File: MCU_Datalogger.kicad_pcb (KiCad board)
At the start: 2 copper layers, 29 parts, among them J1 Conn_01x04_Pin, J2 Conn_01x04_Pin, J3 Conn_01x09_Pin, J4 Conn_02x03_Odd_Even, U1 24LC1025, U2 24LC1025, U3 DS1337S_, U4 ATMEGA328P-AN, Y1 16 MHz, Y2 32.768 KHz

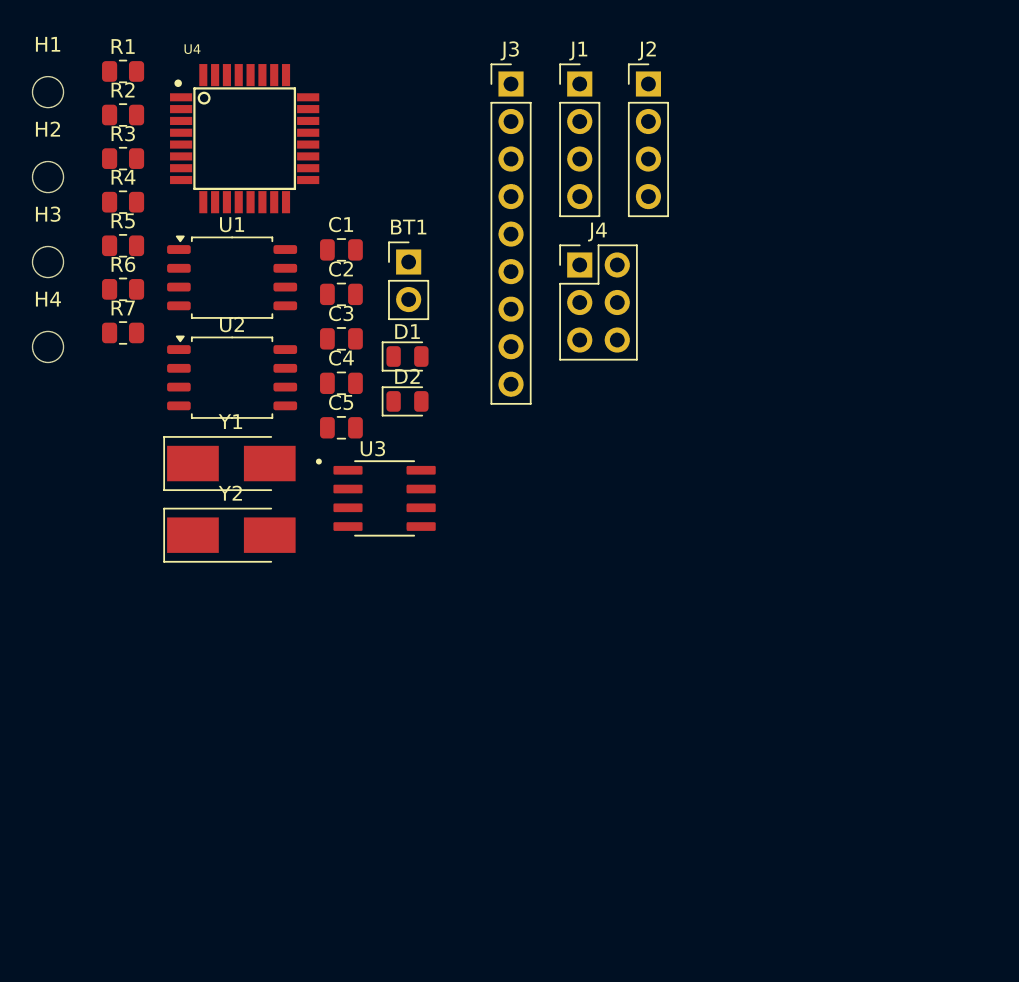
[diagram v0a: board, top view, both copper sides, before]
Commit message: Placed Components in 2 layer PCB.
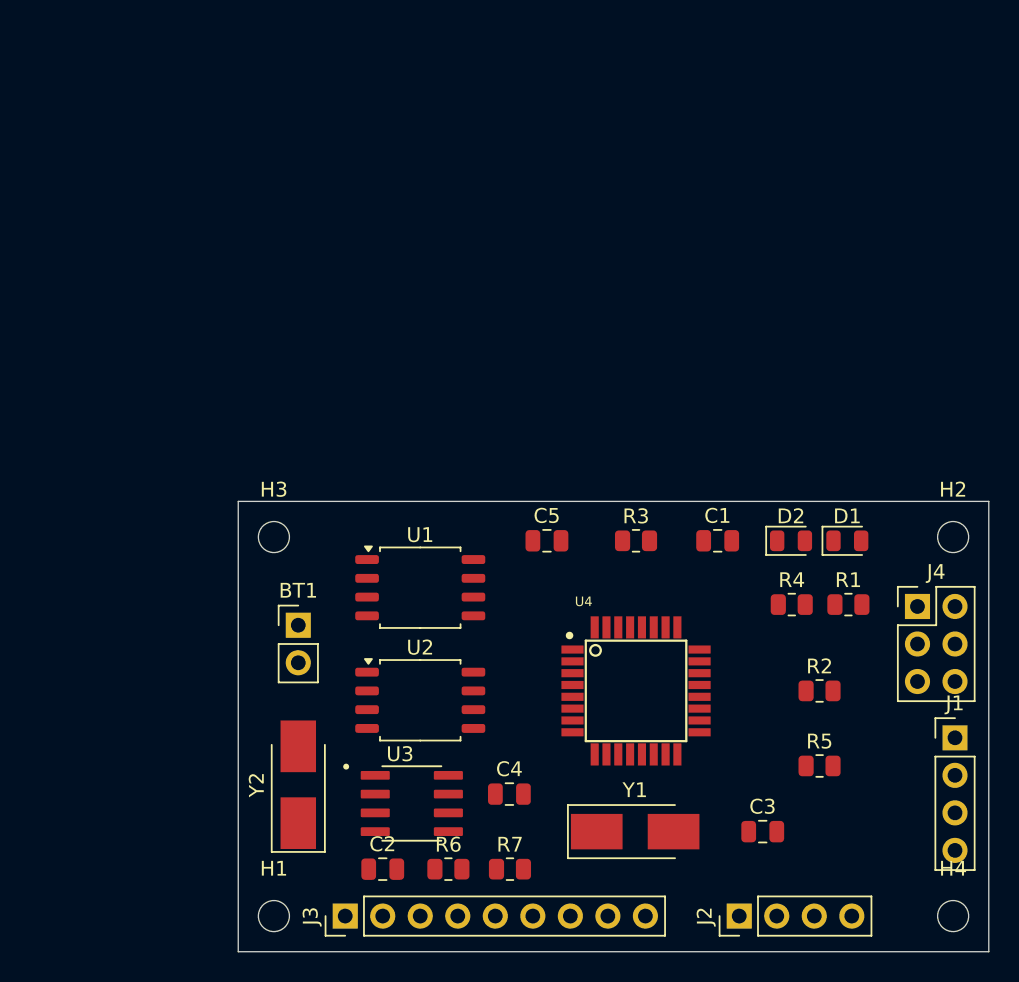
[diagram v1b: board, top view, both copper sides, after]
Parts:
- moved H4 72.4 mm to (173.9, 125.1)
- moved H2 65.9 mm to (173.9, 99.4)
- moved R2 61.2 mm to (164.8, 109.9)
- moved R1 60.9 mm to (166.8, 104.0)
- moved R5 58.8 mm to (164.8, 114.9)
- moved H1 57.8 mm to (127.9, 125.1)
- moved J3 57.4 mm to (132.7, 125.1), turned to 90 degrees
- moved J2 56.7 mm to (159.4, 125.1), turned to 90 degrees
- moved R4 52.8 mm to (162.9, 104.0)
- moved J1 51.0 mm to (174.0, 113.0)
- moved U4 45.8 mm to (152.4, 109.9)
- moved R6 45.0 mm to (139.7, 121.9)
- moved R7 44.8 mm to (143.9, 121.9)
- moved C3 43.9 mm to (161.0, 119.4)
- moved R3 43.3 mm to (152.4, 99.7)
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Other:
- board outline added: 50.8 x 30.5 mm

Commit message: Two Layer PCB Routing Done.
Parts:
- moved R7 16.5 mm to (143.8, 105.4)
- moved R6 8.19 mm to (143.8, 114.8)
- moved C4 7.33 mm to (150.9, 118.9)
- moved Y1 5.08 mm to (157.4, 119.4)
- moved C3 3.81 mm to (164.8, 119.4)
- moved U4 1.46 mm to (153.8, 109.5)
- moved U1 1.38 mm to (137.3, 101.6)
- moved U2 1.38 mm to (137.3, 109.2)
- moved U3 1.27 mm to (137.2, 116.2)
- moved R5 1.01 mm to (165.6, 114.3)
- moved D1 0.94 mm to (167.6, 99.7)
- moved R1 0.87 mm to (167.6, 104.0)
- moved Y2 0.68 mm to (129.0, 115.8)
- moved BT1 0.63 mm to (128.9, 105.4)
- moved C2 0.51 mm to (135.2, 121.4), turned to 180 degrees
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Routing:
- net GND: track 0.00 -> 203.2 mm, vias 0 -> 10
- net /Vcc: track 0.00 -> 167.8 mm, vias 0 -> 10
- net /SCK: track 0.00 -> 106.9 mm, vias 0 -> 12
- net Net-(U4-PB6): track 0.00 -> 95.7 mm, vias 0 -> 6
- net /SDA: track 0.00 -> 93.8 mm, vias 0 -> 6
- net Net-(BT1-+): track 0.00 -> 91.1 mm, vias 0 -> 3
- net /RX: track 0.00 -> 48.3 mm
- net /TX: track 0.00 -> 45.7 mm
- net /MOSI: track 0.00 -> 44.0 mm, vias 0 -> 1
- net /RESET: track 0.00 -> 43.8 mm, vias 0 -> 5
- net Net-(U4-PB7): track 0.00 -> 39.6 mm, vias 0 -> 2
- net /D2: track 0.00 -> 32.7 mm, vias 0 -> 2
- net /D3: track 0.00 -> 27.6 mm, vias 0 -> 2
- net Net-(U4-AREF): track 0.00 -> 26.9 mm
- net /D4: track 0.00 -> 24.5 mm, vias 0 -> 2
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
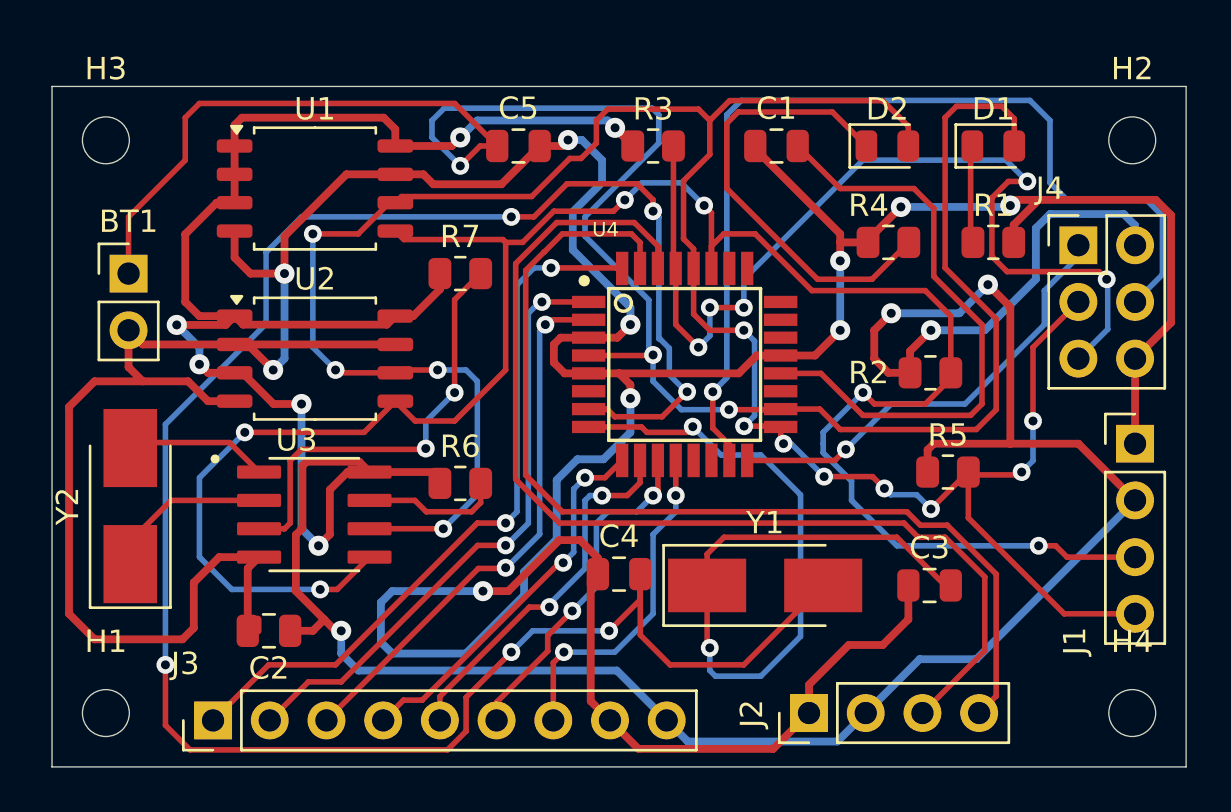
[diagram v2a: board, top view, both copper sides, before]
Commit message: Two Layer PCB done along with 3d Models.
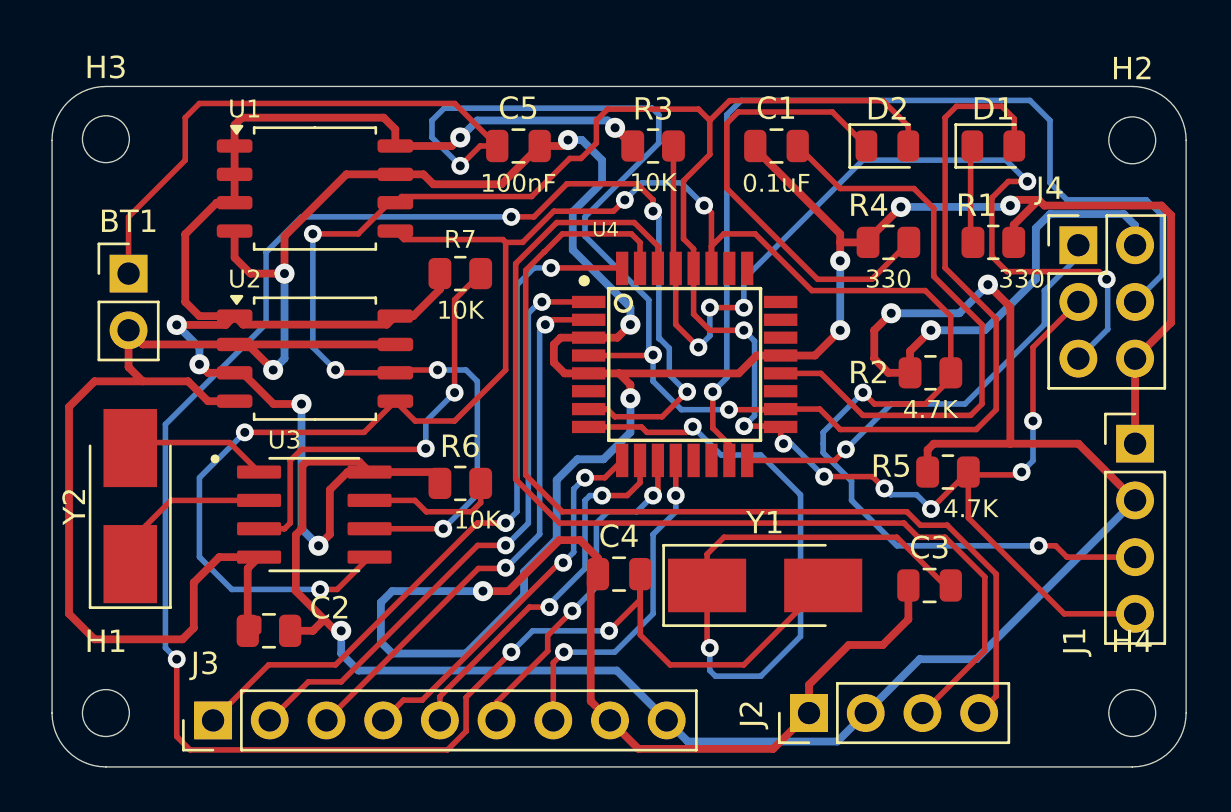
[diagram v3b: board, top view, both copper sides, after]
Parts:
- added REF**: KiCad-Logo2_5mm_SilkScreen, Symbol:KiCad-Logo2_5mm_SilkScreen, B.Cu at (136.9, 100.1)
- moved H3 0.05 mm to (127.9, 99.4)
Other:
- outline, holes or cut-outs redrawn
- board text added: "Dhruv Santosh Warik"
- board text added: "MCU Datalogger with EEPROM and Clock"

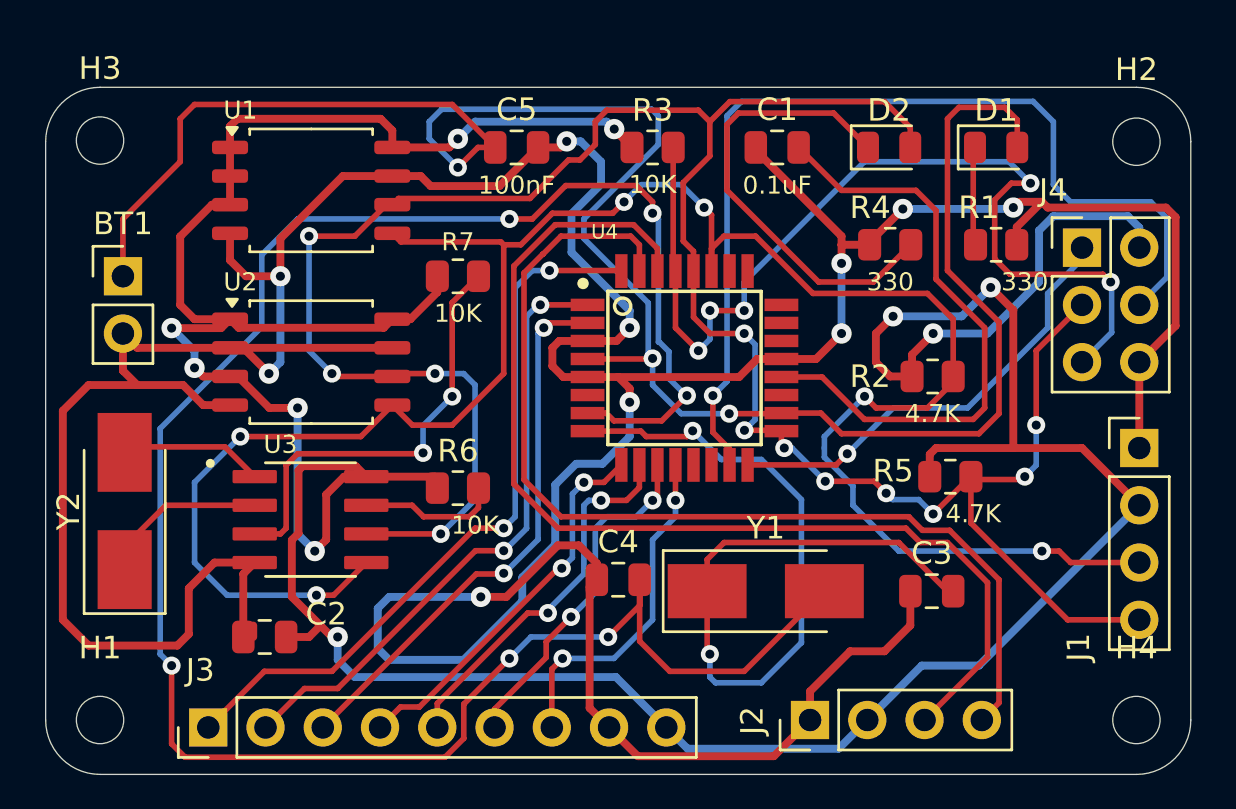
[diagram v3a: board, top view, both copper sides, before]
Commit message: Completed 2 layer PCB MCU along with gerbers.
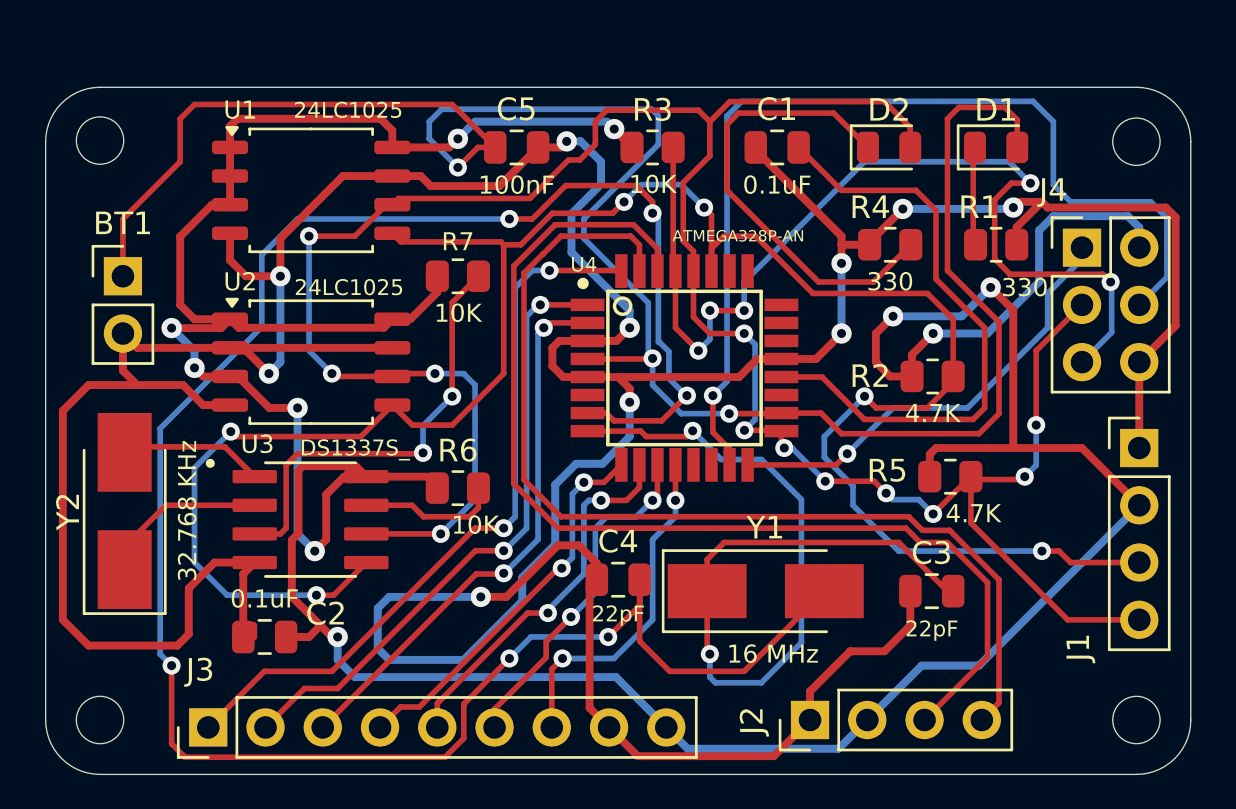
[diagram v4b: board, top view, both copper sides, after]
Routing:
- net /SDA: track 93.8 -> 94.4 mm
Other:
- board text added: "0.2000 mm / 0.0000 mm"
- board text added: "0.3000 mm"
- board text added: "1.6000 mm"
- board text added: "2"
- board text added: "50.8000 mm x 30.4800 mm"
- board text added: "BOARD CHARACTERISTICS"
- board text added: "Board Thickness:"
- board text added: "Board overall dimensions:"
- board text added: "Castellated pads:"
- board text added: "Copper Finish:"
- board text added: "Copper Layer Count:"
- board text added: "Edge card connectors:"
- board text added: "Impedance Control:"
- board text added: "Min hole diameter:"
- board text added: "Min track/spacing:"
- board text added: "No"
- board text added: "None"
- board text added: "Plated Board Edge:"
